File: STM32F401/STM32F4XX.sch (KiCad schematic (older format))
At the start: 32 parts, among them J1 DEBUG UART, J2 Conn_02x16_Counter_Clockwise, J3 USB_B_Mini, J4 Conn_02x16_Counter_Clockwise, J5 JTAG SWDIO SWCLK, SW1 ~RESET, U1 STM32F401RCTx, U2 LM1117-3.3, Y1 8MHz

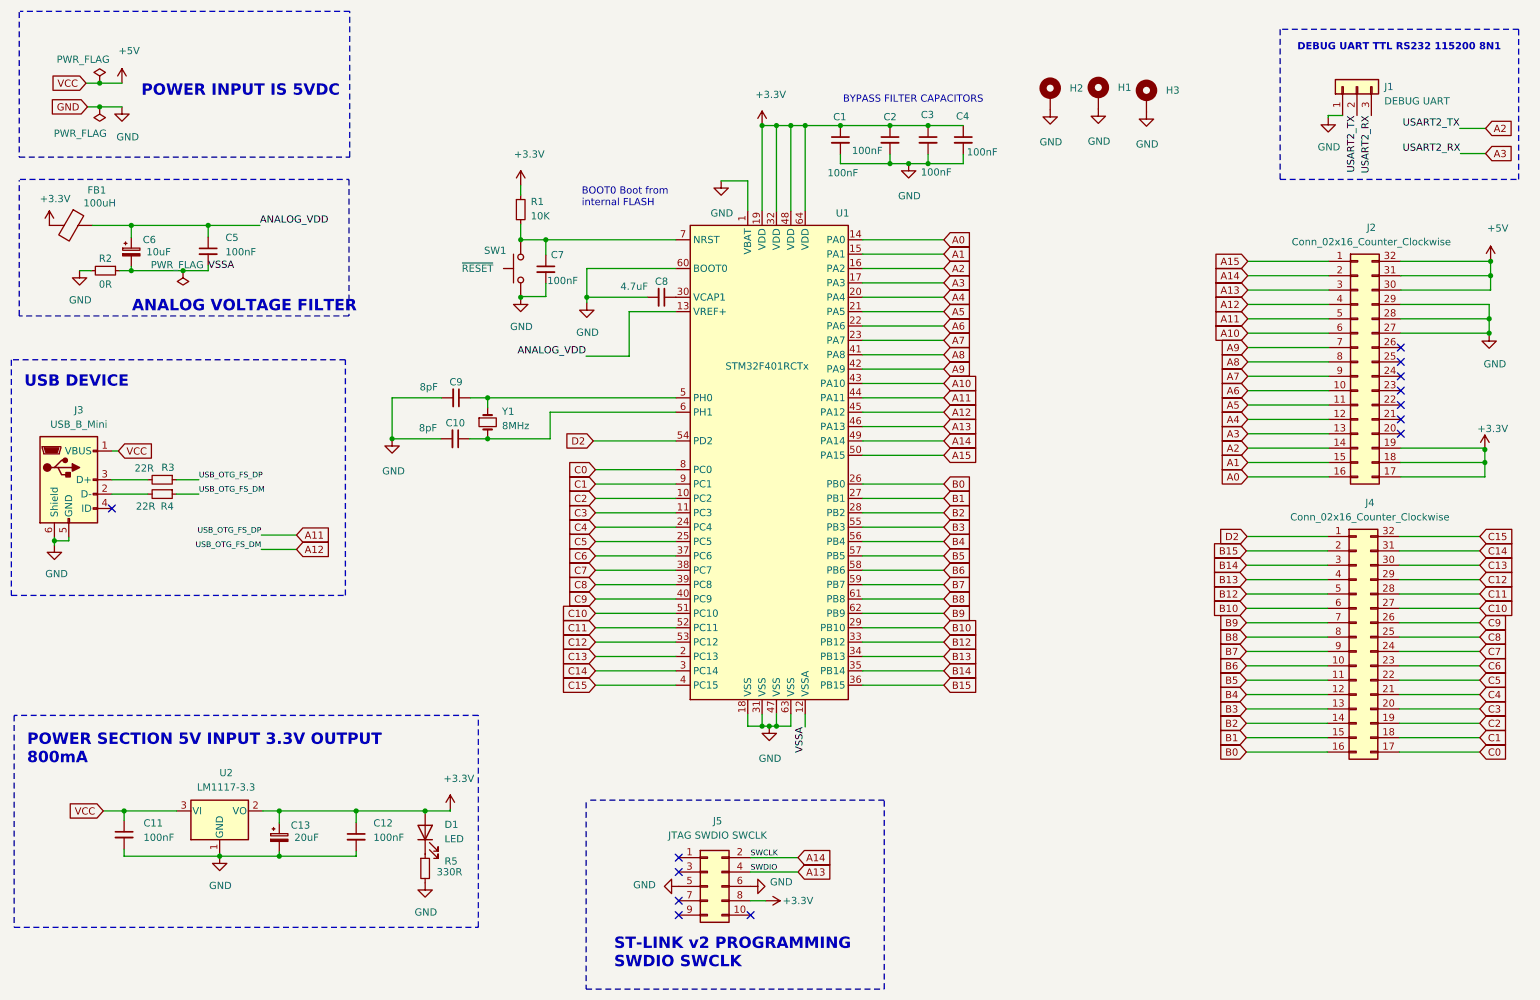
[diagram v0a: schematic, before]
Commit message: Modified for JLCPCB production and added some silkscreens
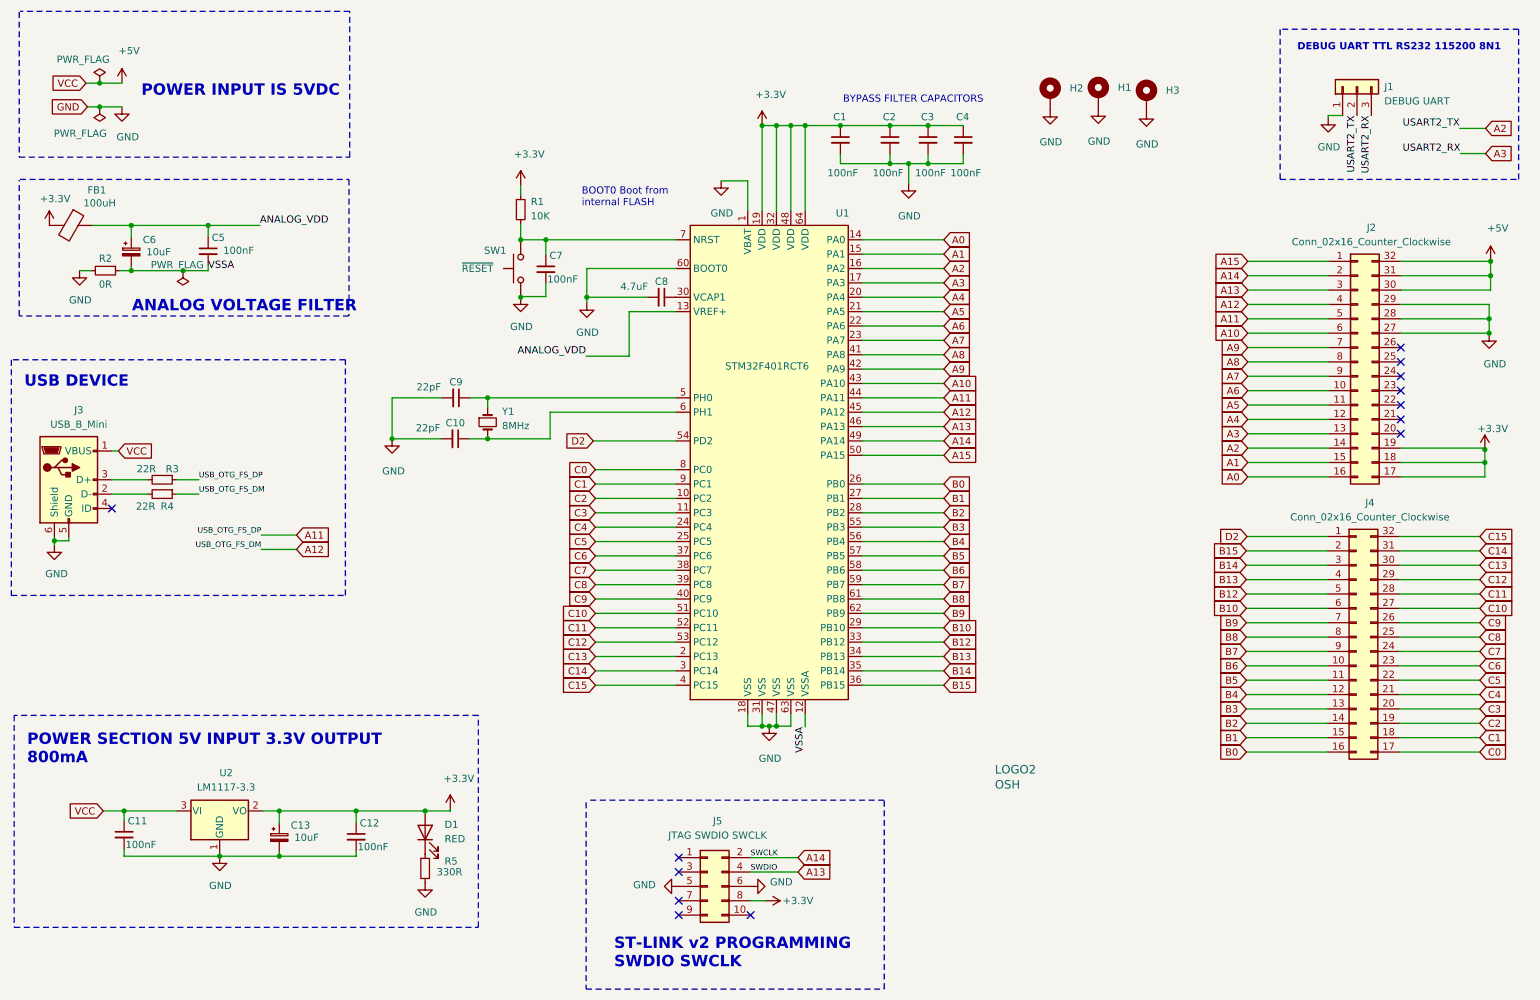
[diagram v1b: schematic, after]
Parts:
- added LOGO2: OSH, Symbol:OSHW-Logo_11.4x12mm_SilkScreen, symbol AmigaComponents:LOGO
- C1, C11, C12, C2, C3, C4, C5, C7: LCSC (none) -> C24497
- C10, C9: value 8pF -> 22pF; footprint Capacitor_SMD:C_01005_0402Metric_Pad0.57x0.30mm_HandSolder -> Capacitor_SMD:C_1206_3216Metric_Pad1.33x1.80mm_HandSolder; LCSC (none) -> C1896
- C13: value 20uF -> 10uF; footprint Capacitor_Tantalum_SMD:CP_EIA-3216-18_Kemet-A_Pad1.58x1.35mm_HandSolder -> Capacitor_Tantalum_SMD:CP_EIA-3216-12_Kemet-S_Pad1.58x1.35mm_HandSolder; LCSC (none) -> C108529
- C6: LCSC (none) -> C108529
- C8: LCSC (none) -> C7237
- D1: value LED -> RED; LCSC (none) -> C93133
- FB1: LCSC (none) -> C128802
- J3: LCSC (none) -> C69074
- R1: LCSC (none) -> C17902
- R2: LCSC (none) -> C17888
- R3, R4: LCSC (none) -> C114943
- R5: LCSC (none) -> C245520
- U1: value STM32F401RCTx -> STM32F401RCT6; LCSC (none) -> C74524
- U2: LCSC (none) -> C126027
- Y1: LCSC (none) -> C107426
